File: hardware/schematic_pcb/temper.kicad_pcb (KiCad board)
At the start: 2 copper layers, 36 x 96.5 mm, 53 parts, among them J1 conn_01x03, J2 conn_01x03, J3 conn_01x03, J4 conn_01x03, J5 Charge Connector, J6 MCU Serial I/F, J7 Conn_01x10, M1 AO3401A, Q1 2N7002, Q2 2N7002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

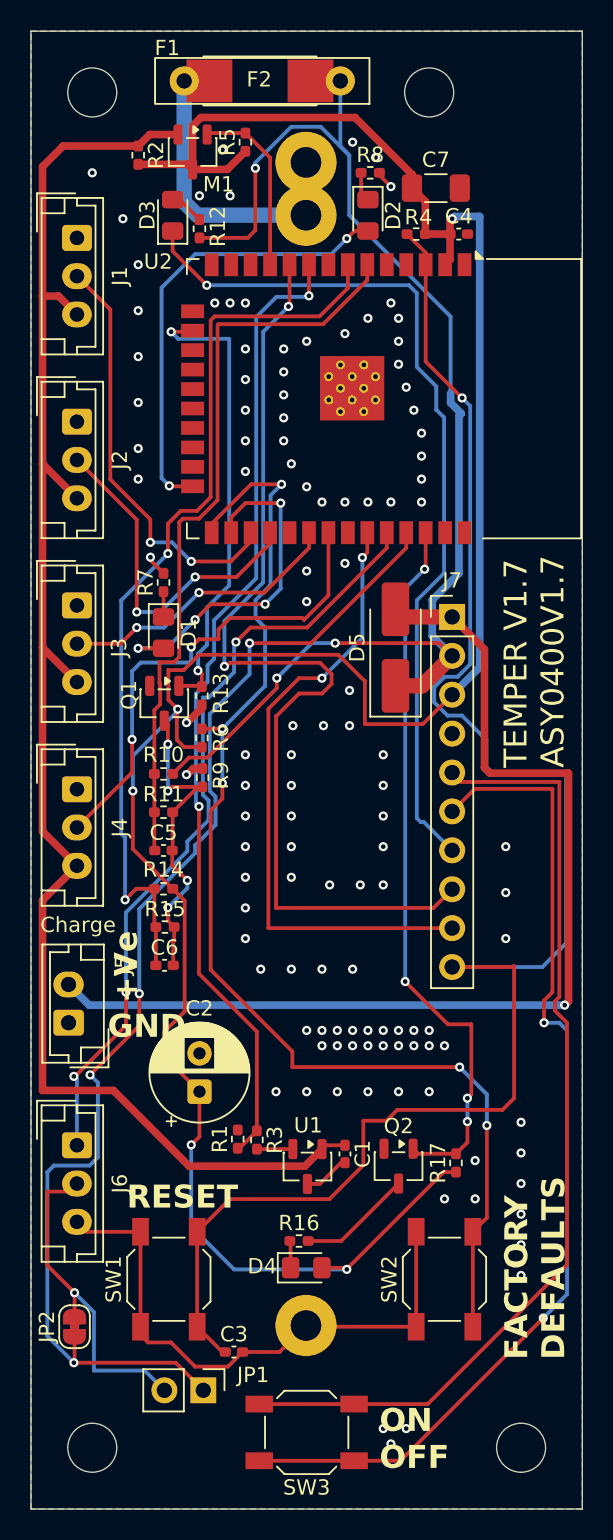
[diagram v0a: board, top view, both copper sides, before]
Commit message: Added cap on DHT22 power. It's unclear if this is needed and these PCB's have not been built as I'm testing the 1.7 PCB to check if the 220uf 25v cap fixes the sensor read lockup for sensors 2 & 3.
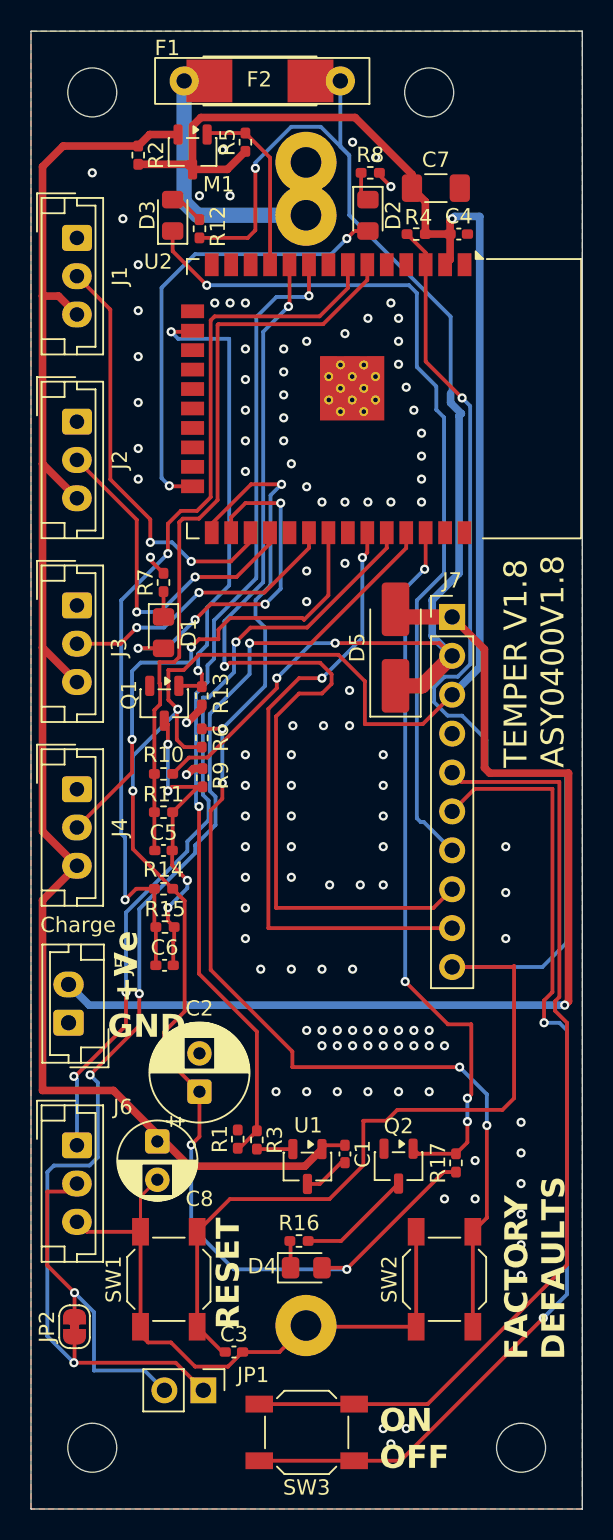
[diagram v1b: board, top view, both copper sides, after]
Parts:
- added C8: 100uf 16v, Capacitor_THT:CP_Radial_D5.0mm_P2.50mm, F.Cu at (138.2, 125.2)
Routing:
- net GND: track 46.1 -> 50.0 mm
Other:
- board text added: "TEMPER V1.8 ASY0400V1.8"
- board text removed: "TEMPER V1.7 ASY0400V1.7"

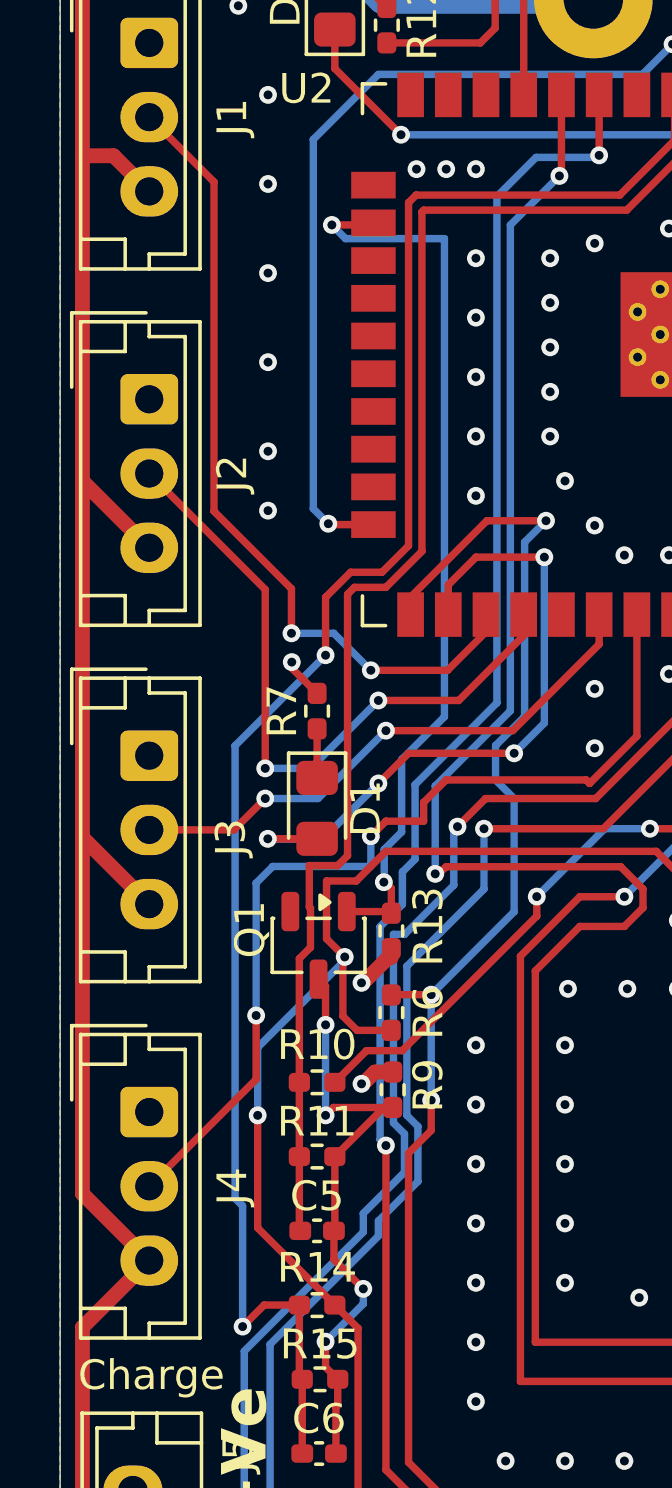
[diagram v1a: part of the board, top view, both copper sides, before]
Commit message: Add pullup resistors on DHT22 data lines as temp readings were not reliable.
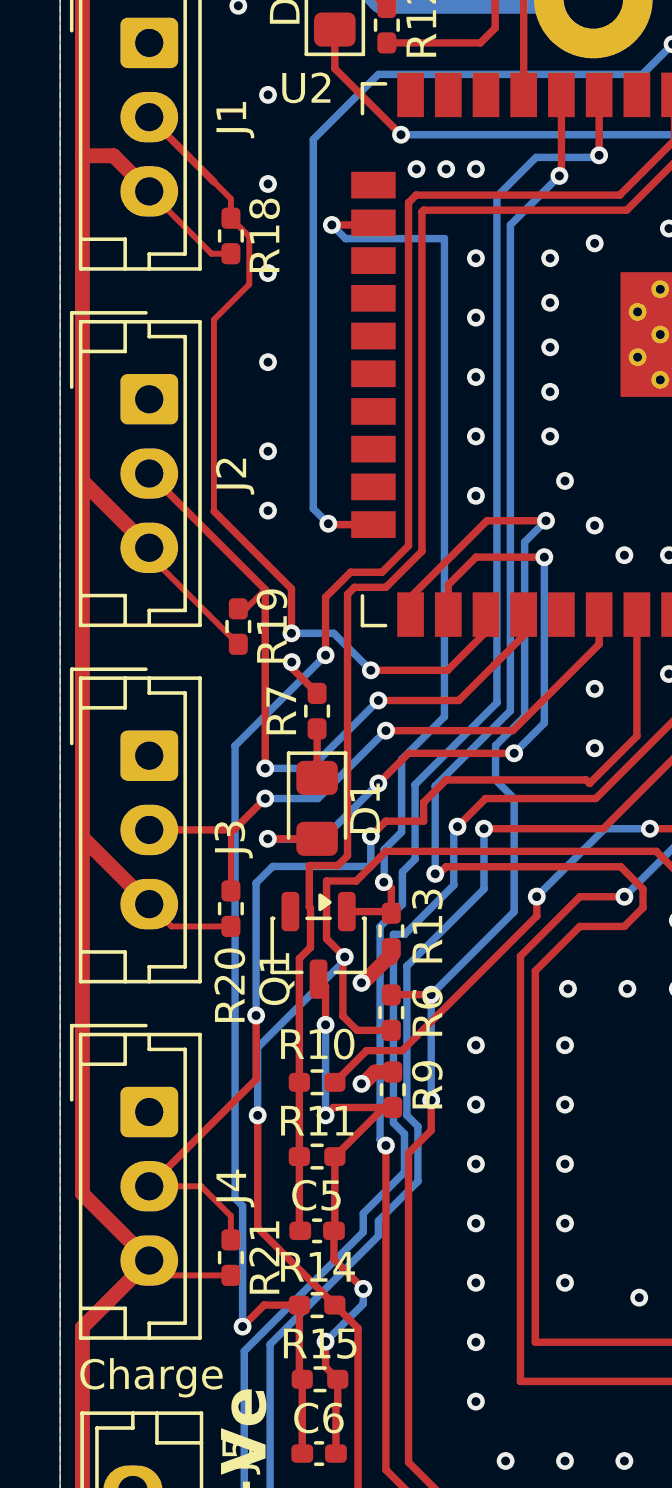
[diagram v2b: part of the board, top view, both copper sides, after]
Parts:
- added R18: 1k, Resistor_SMD:R_0402_1005Metric_Pad0.72x0.64mm_HandSolder, F.Cu at (135.8, 72.8)
- added R19: 1k, Resistor_SMD:R_0402_1005Metric_Pad0.72x0.64mm_HandSolder, F.Cu at (136.0, 85.9)
- added R20: 1k, Resistor_SMD:R_0402_1005Metric_Pad0.72x0.64mm_HandSolder, F.Cu at (135.8, 95.4)
- added R21: 1k, Resistor_SMD:R_0402_1005Metric_Pad0.72x0.64mm_HandSolder, F.Cu at (135.8, 107.2)
- C2: value DNF -> 220uf 25v
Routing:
- net Net-(J1-Pin_3): track 103.8 -> 118.0 mm
- net /DHT22_4: track 31.7 -> 35.7 mm
- net /DHT22_3: track 18.7 -> 20.8 mm
- net /DHT22_2: track 22.8 -> 24.0 mm
- net /DHT22_1: track 27.5 -> 28.5 mm

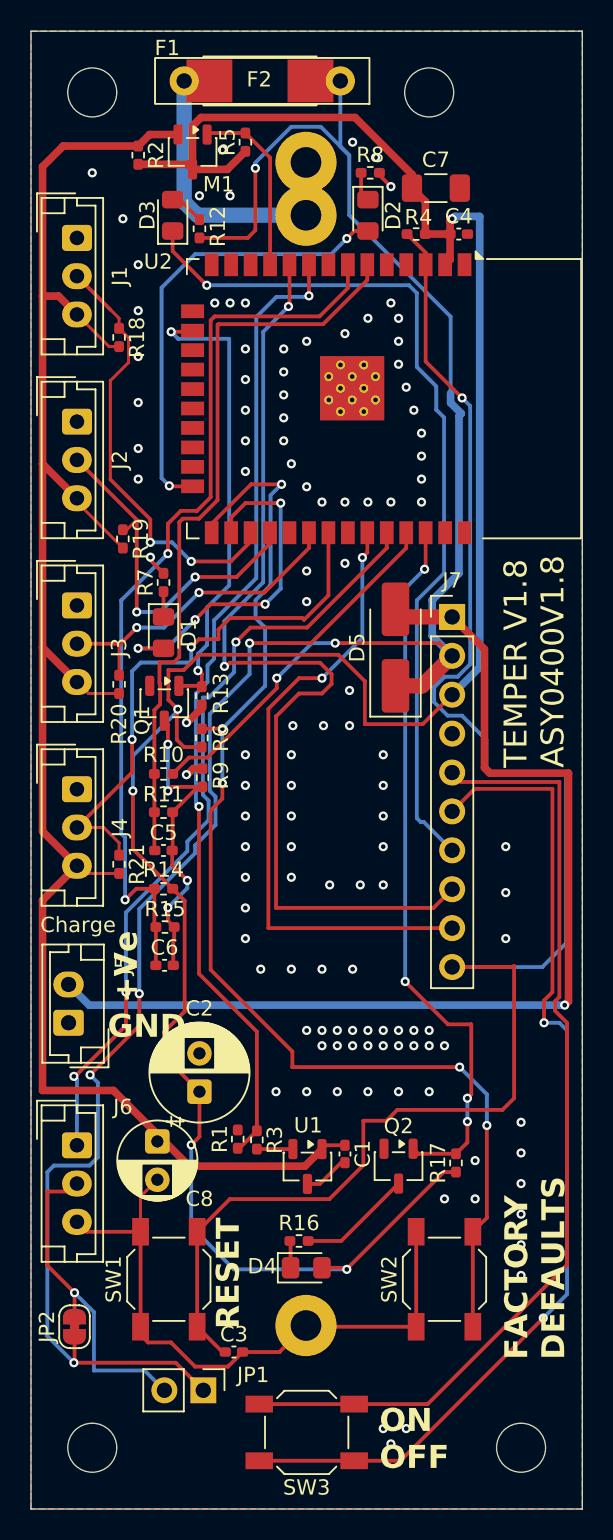
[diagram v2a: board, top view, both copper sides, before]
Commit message: Spin PCB: Power sensors from 5v (3.3v pullups) to allow sensors to sit on the end of longer cables without locking up.
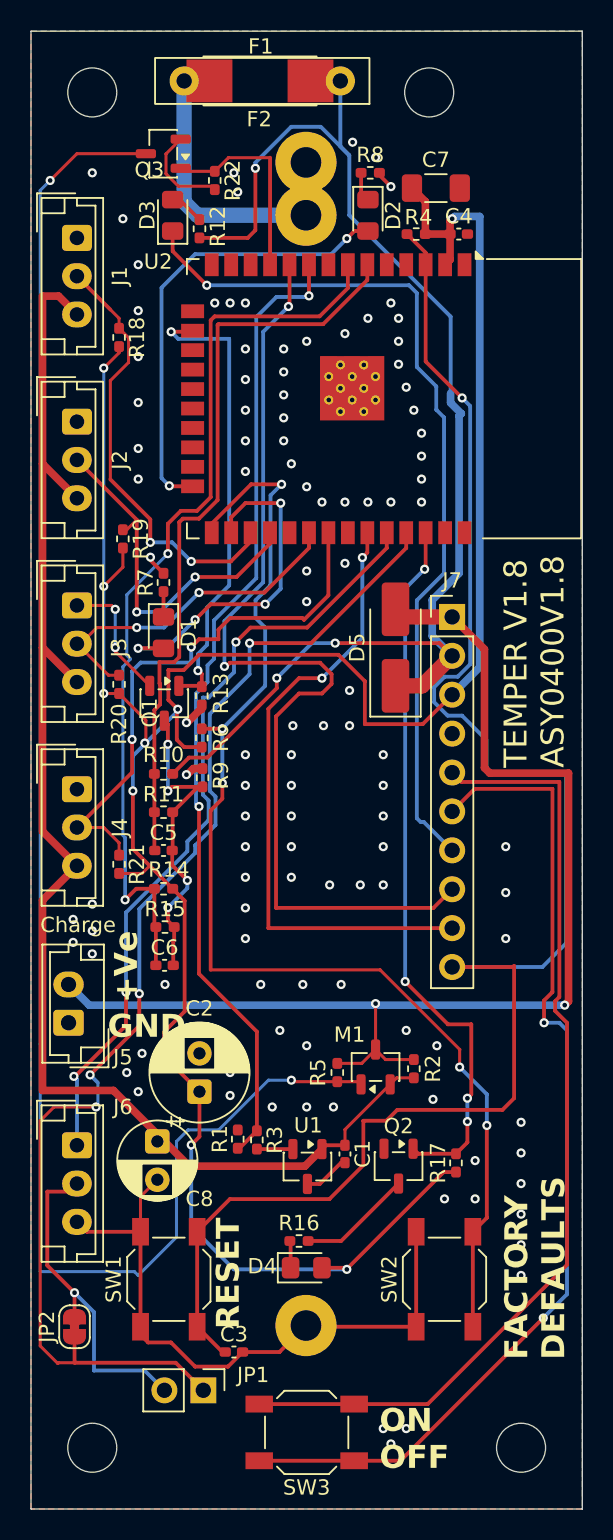
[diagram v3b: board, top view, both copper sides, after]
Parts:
- added Q3: 2N7002, Package_TO_SOT_SMD:SOT-23-3, F.Cu at (138.6, 60.8)
- added R22: 100k, Resistor_SMD:R_0402_1005Metric_Pad0.72x0.64mm_HandSolder, F.Cu at (142.0, 62.5)
- R18, R19, R20, R21: value 1k -> 4k7
- R2: value DNF -> 0R
- moved R2 62.3 mm to (155.0, 120.5), turned to 90 degrees
- moved R5 61.0 mm to (150.0, 120.8), turned to -90 degrees
- moved M1 60.9 mm to (152.5, 120.4), turned to 90 degrees
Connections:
- M1 pad 1: //TON -> Net-(M1-G1)
- M1 pad 3: 3v3 -> +5v
- R18 pad 2: Net-(J1-Pin_3) -> 3v3
- R19 pad 2: Net-(J1-Pin_3) -> 3v3
- R2 pad 2: 3v3 -> +5v
- R20 pad 2: Net-(J1-Pin_3) -> 3v3
- R21 pad 2: Net-(J1-Pin_3) -> 3v3
- R5 pad 1: 3v3 -> +5v
- R5 pad 2: //TON -> Net-(M1-G1)
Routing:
- net Net-(M1-G1): track 0.00 -> 108.6 mm, vias 0 -> 2
- net Net-(J1-Pin_3): track 118.0 -> 93.5 mm
- net GND: track 50.0 -> 64.8 mm, vias 118 -> 114
- net +5v: track 68.5 -> 77.1 mm, vias 1 -> 2
- net 3v3: track 160.4 -> 166.2 mm, vias 5 -> 9
- net /DHT22_3: track 20.8 -> 22.3 mm
- net //TON: track 11.8 -> 13.3 mm
- net /TXD: track 80.4 -> 81.7 mm

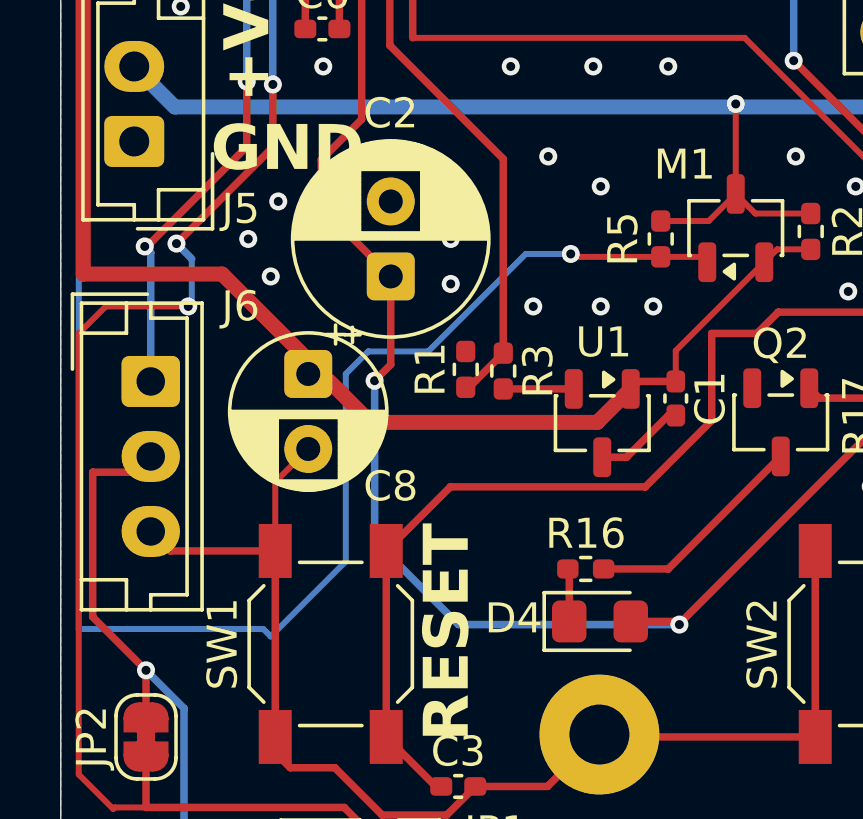
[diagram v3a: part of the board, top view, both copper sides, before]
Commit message: Moved C2 on PCB as there was too close to J5
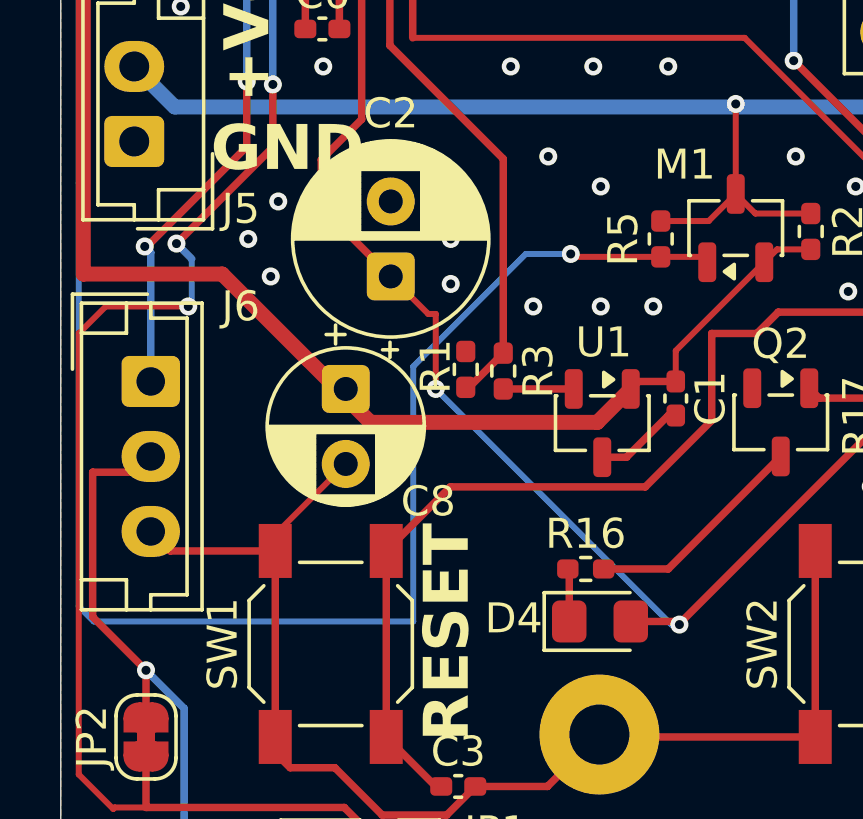
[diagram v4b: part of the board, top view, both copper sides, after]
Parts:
- R2: value 0R -> DNF
- moved C8 1.35 mm to (139.5, 125.8)
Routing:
- net 3v3: track 166.2 -> 161.8 mm
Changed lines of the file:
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@@
 	(title_block
 		(title "Temper (temperature monitoring device).")
-		(date "2026-04-20")
-		(rev "1.8")
+		(date "2026-05-14")
+		(rev "1.9")
 	)
 	(layers
@@
 			)
 		)
-		(property "LCSC" "C17168"
+		(property "LCSC" "C25900"
 			(at 0 0 270)
 			(unlocked yes)
@@
 			)
 		)
-		(property "Value" "0R"
+		(property "Value" "DNF"
 			(at 0 1.17 90)
 			(layer "F.Fab")
@@
 			)
 		)
-		(property "LCSC" "C17168"
+		(property "LCSC" "C25900"
 			(at 0 0 270)
 			(unlocked yes)
@@
 	(footprint "Capacitor_THT:CP_Radial_D5.0mm_P2.50mm"
 		(layer "F.Cu")
-		(at 138.25 125.25 -90)
+		(at 139.5 125.75 -90)
 		(descr "CP, Radial series, Radial, pin pitch=2.50mm, diameter=5mm, height=7mm, Electrolytic Capacitor")
 		(tags "CP Radial series Radial pin pitch 2.50mm diameter 5mm height 7mm Electrolytic Capacitor")
@@
 			)
 		)
-		(property "LCSC" "C17168"
+		(property "LCSC" "C25900"
 			(at 0 0 270)
 			(unlocked yes)
@@
 		(tags "resistor handsolder")
 		(property "Reference" "R1"
-			(at 0 -1.17 90)
+			(at 0.0975 -1 90)
 			(layer "F.SilkS")
 			(effects
@@
 			)
 		)
-		(property "LCSC" "C17168"
+		(property "LCSC" "C25900"
 			(at 0 0 270)
 			(unlocked yes)
@@
 	)
 	(segment
-		(start 138.25 127.75)
-		(end 137.15 128.85)
-		(width 0.2)
-		(layer "F.Cu")
-		(net 2)
-	)
-	(segment
 		(start 143.8175 139)
 		(end 142.8635 139.954)
@@
 	)
 	(segment
-		(start 137.15 128.85)
-		(end 137.15 131.15)
-		(width 0.2)
-		(layer "F.Cu")
-		(net 2)
-	)
-	(segment
 		(start 152.75 62.15)
 		(end 153.5 62.9)
@@
 	)
 	(segment
+		(start 137.15 130.6)
+		(end 137.15 131.15)
+		(width 0.2)
+		(layer "F.Cu")
+		(net 2)
+	)
+	(segment
 		(start 148.035 137.35)
 		(end 147.955 137.27)
@@
 	)
 	(segment
+		(start 139.5 128.25)
+		(end 137.15 130.6)
+		(width 0.2)
+		(layer "F.Cu")
+		(net 2)
+	)
+	(segment
 		(start 138.8125 60.7625)
 		(end 138.8125 62.0625)
@@
 	)
 	(segment
+		(start 142.25 123.25)
+		(end 141 122)
+		(width 0.2)
+		(layer "F.Cu")
+		(net 3)
+	)
+	(segment
 		(start 140.031 109.531)
 		(end 140.031 116.763)
@@
 	)
 	(segment
+		(start 142.5 125.75)
+		(end 142.5 123.25)
+		(width 0.2)
+		(layer "F.Cu")
+		(net 3)
+	)
+	(segment
 		(start 139.522 97.089)
 		(end 139.583 97.028)
@@
 	)
 	(segment
-		(start 141 124.938)
-		(end 140.462 125.476)
-		(width 0.25)
-		(layer "F.Cu")
-		(net 3)
-	)
-	(segment
 		(start 136.652 106.152)
 		(end 136.652 102.362)
@@
 	)
 	(segment
-		(start 141 122)
-		(end 141 124.938)
-		(width 0.25)
-		(layer "F.Cu")
-		(net 3)
-	)
-	(segment
 		(start 155.75 63.875)
 		(end 154.875 63)
@@
 	)
 	(segment
+		(start 142.5 123.25)
+		(end 142.25 123.25)
+		(width 0.2)
+		(layer "F.Cu")
+		(net 3)
+	)
+	(segment
 		(start 137.5 99.25)
 		(end 137.441 99.25)
@@
 	)
 	(via
-		(at 140.462 125.476)
+		(at 157.5 65)
 		(size 0.6)
 		(drill 0.3)
@@
 	)
 	(via
-		(at 157.5 65)
+		(at 134.75 96)
 		(size 0.6)
 		(drill 0.3)
@@
 	)
 	(via
-		(at 134.75 96)
+		(at 134.75 74.75)
 		(size 0.6)
 		(drill 0.3)
@@
 	)
 	(via
-		(at 134.75 74.75)
+		(at 142.5 125.75)
 		(size 0.6)
 		(drill 0.3)
@@
 	)
 	(segment
-		(start 140.462 130.81)
-		(end 143.256 133.604)
-		(width 0.25)
-		(layer "B.Cu")
-		(net 3)
-	)
-	(segment
 		(start 136.652 102.362)
 		(end 136.652 100.076)
@@
 	)
 	(segment
+		(start 150.354 133.604)
+		(end 150.622 133.604)
+		(width 0.2)
+		(layer "B.Cu")
+		(net 3)
+	)
+	(segment
 		(start 134.75 89)
 		(end 134.75 74.75)
@@
 	)
 	(segment
+		(start 142.5 125.75)
+		(end 150.354 133.604)
+		(width 0.2)
+		(layer "B.Cu")
+		(net 3)
+	)
+	(segment
 		(start 157.65 64.85)
 		(end 157.5 65)
@@
 	)
 	(segment
-		(start 143.256 133.604)
-		(end 150.622 133.604)
-		(width 0.25)
-		(layer "B.Cu")
-		(net 3)
-	)
-	(segment
 		(start 136.652 100.076)
 		(end 139.7 97.028)
@@
 	)
 	(segment
-		(start 140.462 125.476)
-		(end 140.462 130.81)
-		(width 0.25)
-		(layer "B.Cu")
-		(net 3)
-	)
-	(segment
 		(start 134.75 89)
 		(end 134.75 96)
@@
 	)
 	(segment
-		(start 138.25 125.25)
-		(end 138.25 124.788)
-		(width 0.2)
-		(layer "F.Cu")
-		(net 9)
-	)
-	(segment
 		(start 130.751 109.499)
 		(end 130.751 121.92)
@@
 	)
 	(segment
-		(start 130.6 133.75)
-		(end 130.6 118.884744)
+		(start 141.75 125)
+		(end 141.75 133.5)
 		(width 0.2)
 		(layer "B.Cu")
@@
 	)
 	(segment
-		(start 131.25 62.5)
-		(end 130.6 63.15)
+		(start 130.6 133)
+		(end 130.6 118.884744)
 		(width 0.2)
 		(layer "B.Cu")
@@
 	)
 	(segment
-		(start 139.5 125.25)
-		(end 139.5 131.5)
+		(start 141.75 133.5)
+		(end 131.1 133.5)
 		(width 0.2)
 		(layer "B.Cu")
@@
 	)
 	(segment
-		(start 140.25 124.5)
-		(end 139.5 125.25)
+		(start 145.5 121.25)
+		(end 141.75 125)
 		(width 0.2)
 		(layer "B.Cu")
@@
 	)
 	(segment
-		(start 130.6 63.15)
-		(end 130.6 118.884744)
-		(width 0.2)
-		(layer "B.Cu")
-		(net 52)
-	)
-	(segment
-		(start 139.5 131.5)
-		(end 137 134)
-		(width 0.2)
-		(layer "B.Cu")
-		(net 52)
-	)
-	(segment
-		(start 142.25 124.5)
-		(end 140.25 124.5)
-		(width 0.2)
-		(layer "B.Cu")
-		(net 52)
-	)
-	(segment
-		(start 137 134)
-		(end 136.75 133.75)
+		(start 131.25 62.5)
+		(end 130.6 63.15)
 		(width 0.2)
 		(layer "B.Cu")
@@
 	)
 	(segment
-		(start 145.5 121.25)
-		(end 142.25 124.5)
+		(start 131.1 133.5)
+		(end 130.6 133)
 		(width 0.2)
 		(layer "B.Cu")
@@
 	)
 	(segment
-		(start 136.75 133.75)
-		(end 130.6 133.75)
+		(start 130.6 63.15)
+		(end 130.6 118.884744)
 		(width 0.2)
 		(layer "B.Cu")

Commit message: /TON changed to TON for latest SCHEMATIC/PCB
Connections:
- net //TON renamed /TON
